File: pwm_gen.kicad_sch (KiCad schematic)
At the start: 63 parts, among them J2 FAN, J3 STAND, J4 68000-103HLF, Q1 BC847, Q2 2N7002, U1 NE556, U2 NE555D

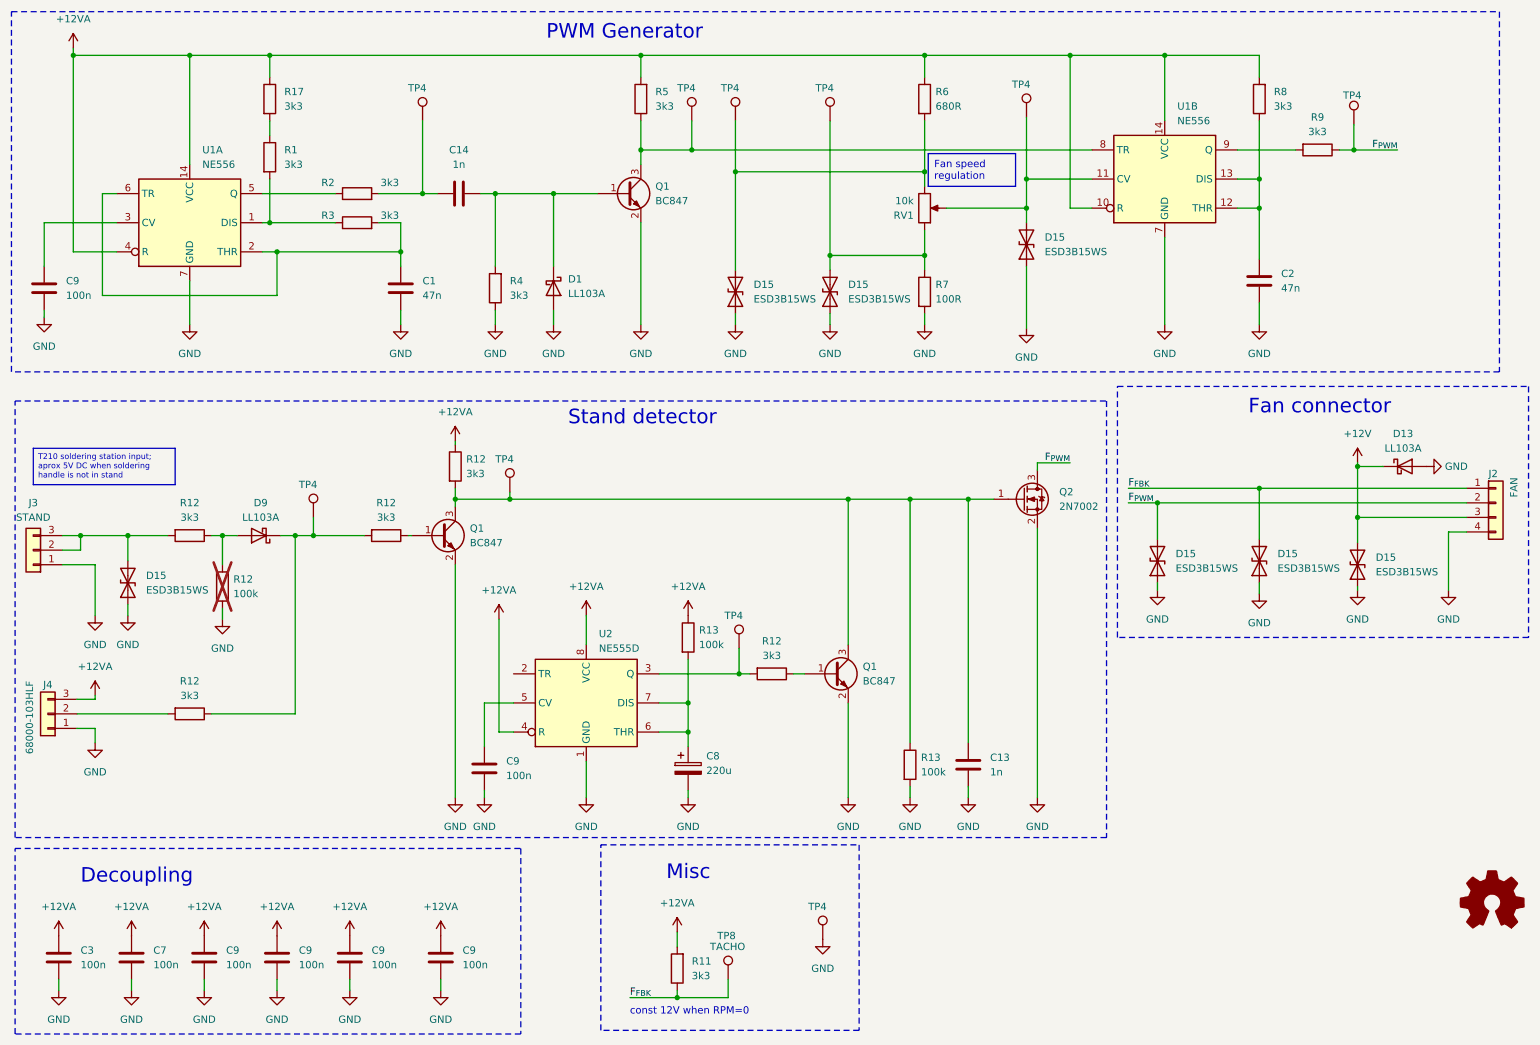
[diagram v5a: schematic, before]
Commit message: Fix U2 treshold circuit
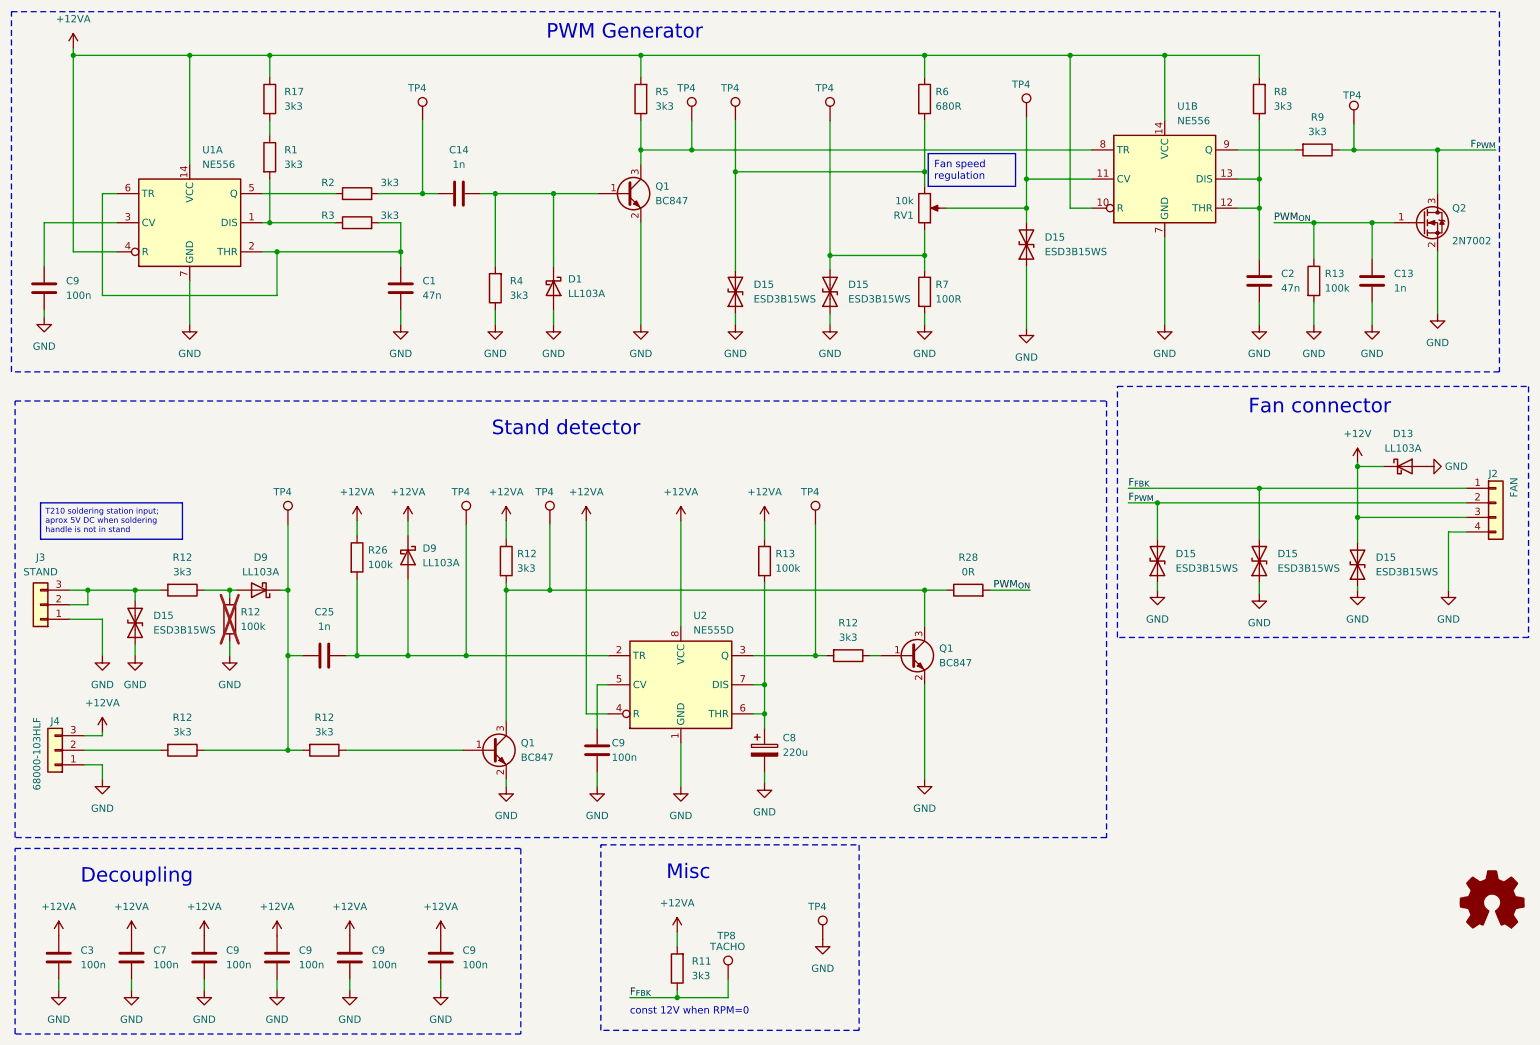
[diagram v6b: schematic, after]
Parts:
- added C25: 1n, Capacitor_SMD:C_0603_1608Metric, symbol CAP_CER_WALSIN_0603:CAP_1n_X7R
- added D9: LL103A, Diode_SMD:D_MiniMELF, symbol Shottky_diodes:LL103A
- added R26: 100k, Resistor_SMD:R_0603_1608Metric, symbol RES_YAGEO_RC0603:RES_100k_0603
- added R28: 0R, Resistor_SMD:R_0603_1608Metric_Pad0.98x0.95mm_HandSolder, symbol Device:R
- added TP4: ~, TestPoint:TestPoint_Pad_D1.0mm, symbol Connector:TestPoint
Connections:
- net +12VA: now also D9.1 (K), R26.1
- net at Q1.3 (C), Q1.3 (C), R12.2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: now also R28.1; no longer C13.2, Q2.1 (G), R13.1
- net at D9.1 (K), R12.1, R12.2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: now also C25.1
- net at U2.2 (TR): now also C25.2, D9.2 (A), R26.2, TP4.1
- new net PWM_{ON}: C13.2, Q2.1 (G), R13.1, R28.2
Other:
- moved on the sheet: C13, C8, C9, D15, D9, J3, J4, Q1, Q2, R12, R13, TP4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
